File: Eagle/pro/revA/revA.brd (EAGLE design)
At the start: 100 x 100 mm, 24 parts, among them Q1 20MHz

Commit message: simplify
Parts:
- added C5, C7, C8, C9: (no value), SparkFun:0805
- added R11, R12, R13: (no value), SparkFun:1206
- added R5: 100K, SparkFun:1206
- added U$4: LM393, SparkFun:SO08
- added U1: MCP42XXX, SparkFun:SO014
- added X1: USB-MB-H, SparkFun:USB-MB-H
- C4, C6: value 22pF -> (none)
- R10: value 100K -> (none)
- U$2: value LM393 -> AUDIO-JACKPTH; device SparkFun:SO08 -> SparkFun:AUDIO-JACK
- moved R8 94.9 mm to (0.00, -23.0)
- moved C6 92.7 mm to (-13.0, -30.0)
- moved R7 85.5 mm to (0.00, -19.0)
- moved C4 80.4 mm to (-2.00, -15.0), turned to 0 degrees
- moved U$2 80.0 mm to (4.00, 20.0)
- moved R6 53.4 mm to (3.00, -15.0)
- moved R10 39.8 mm to (48.0, 46.0)
- moved C2 32.4 mm to (47.0, 13.0), turned to 0 degrees
- moved C3 32.2 mm to (52.0, 13.0), turned to 180 degrees
- moved Q1 21.1 mm to (48.0, 19.0), turned to 0 degrees
- moved R4 16.3 mm to (71.0, 19.0)
- moved U$1 12.0 mm to (82.0, 29.0)
- moved U$3 1.00 mm to (96.0, 20.0)
- turned ATSAM4LS to 270 degrees
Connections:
- new net DIGI_POT_RST: U1.11
- new net DIGI_POT_SHDW: U1.12
- new net DIGI_RES_LEFT: R4.1, U$1.2, U1.7
- new net DIGI_RES_RIGHT: R9.1, U$1.6, U1.8
- new net DIG_POT_CS: U1.1
- new net MISO: ATSAM4LS.25, U1.13
- new net MOSI: ATSAM4LS.26, U1.3
- new net N$13: R13.1
- new net N$14: R12.1
- new net RAW_LEFT: C4.1, U$3.5
- new net RAW_RIGHT: C5.1, U$3.2
- new net SCLK: ATSAM4LS.27, U1.2
- new net USB_D+: ATSAM4LS.47, R10.1
- new net USB_D-: ATSAM4LS.46, R11.1
- new net V+: U$4.8
- new net V-: U$4.4
- new net VCC: R5.2, R8.2, U$1.8, U1.14, X1.VBUS
- net GND: now also C7.2, R7.1, U$1.4, U$2.1, U1.10, U1.4, U1.5, U1.6, U1.9, X1.GND; no longer C4.2, R10.1
- net N$10: now also C6.1, R13.2, U$4.3; no longer U$1.4, U$2.4
- net N$11: now also C7.1, R12.2, U$4.5; no longer U$1.8, U$2.8
- net N$12: now also C8.2, U$2.5; no longer U$2.3, U$3.2
- net N$3: now also R11.2, X1.D-; no longer U$2.5, U$3.5
- net N$4: now also R10.2, X1.D+; no longer R4.1, R6.2, U$1.2
- net N$5: now also C5.2, R7.2; no longer C6.1
- net N$6: now also C4.2, R5.1, R6.2; no longer C4.1, R7.1
- net N$7: now also C9.1, U$4.6, U$4.7; no longer R8.2, U$2.6, U$2.7
- net N$8: now also C9.2; no longer R7.2, U$2.1
- net N$9: now also C8.1, U$4.1, U$4.2; no longer R10.2, R9.1, U$1.6

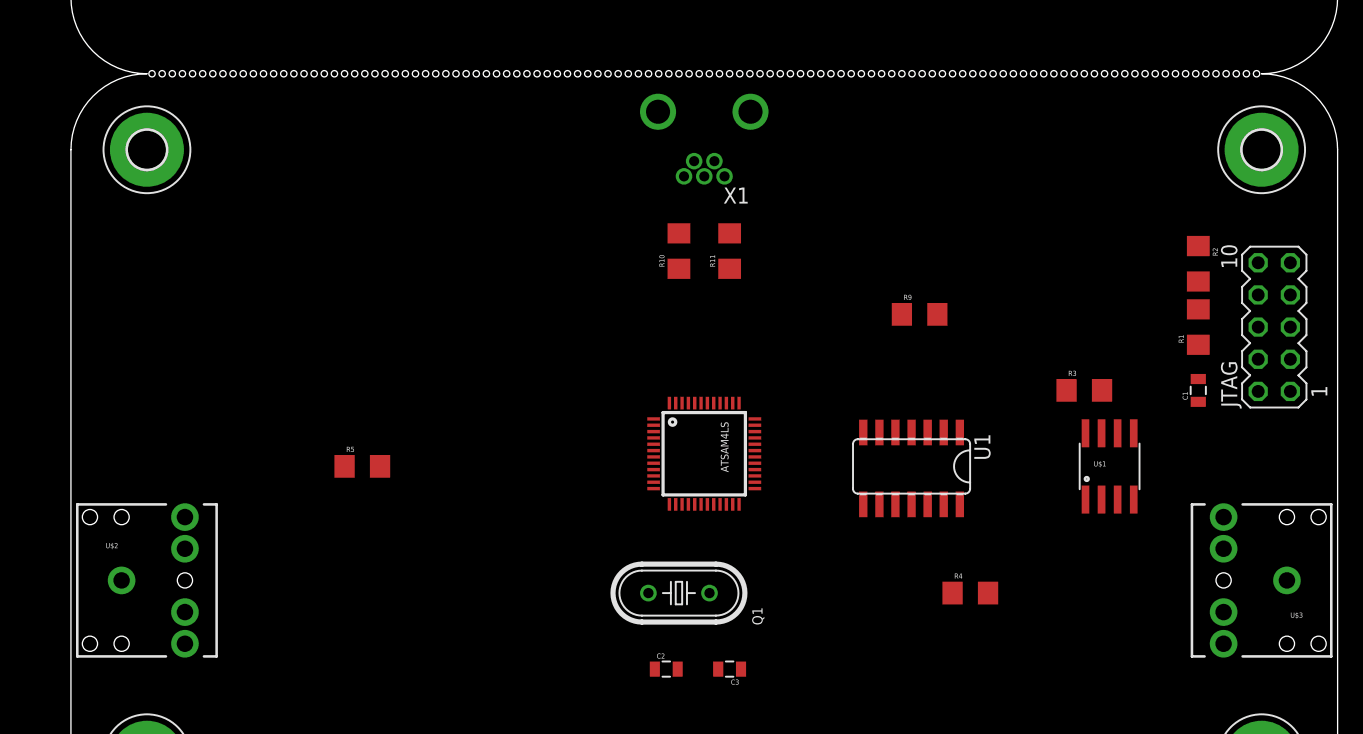
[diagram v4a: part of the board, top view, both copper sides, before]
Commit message: leave jack at the back
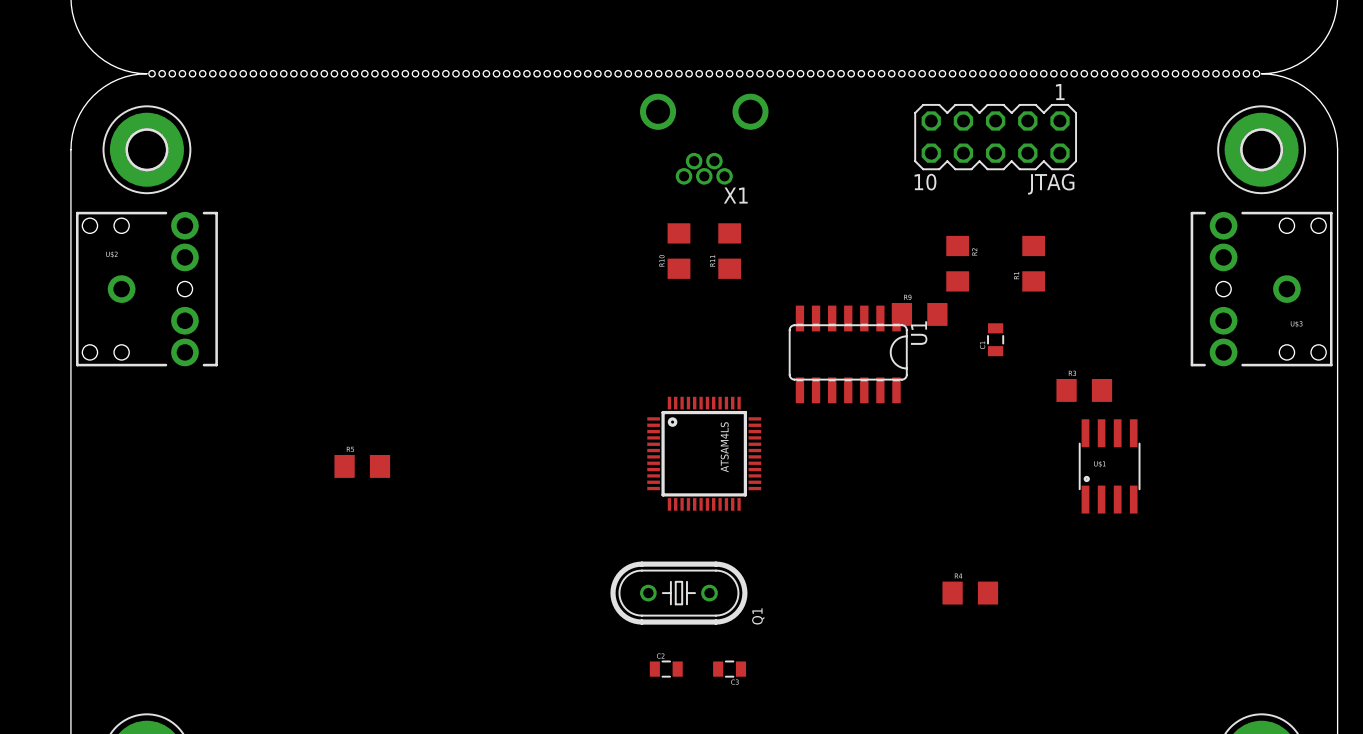
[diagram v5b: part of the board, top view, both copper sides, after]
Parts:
- moved JTAG 26.6 mm to (73.0, 55.0), turned to 180 degrees
- moved U$2 23.0 mm to (4.00, 43.0)
- moved U$3 23.0 mm to (96.0, 43.0)
- moved R2 19.0 mm to (70.0, 45.0)
- moved C1 16.5 mm to (73.0, 39.0)
- moved R1 13.9 mm to (76.0, 45.0)
- moved U1 10.3 mm to (62.0, 38.0)

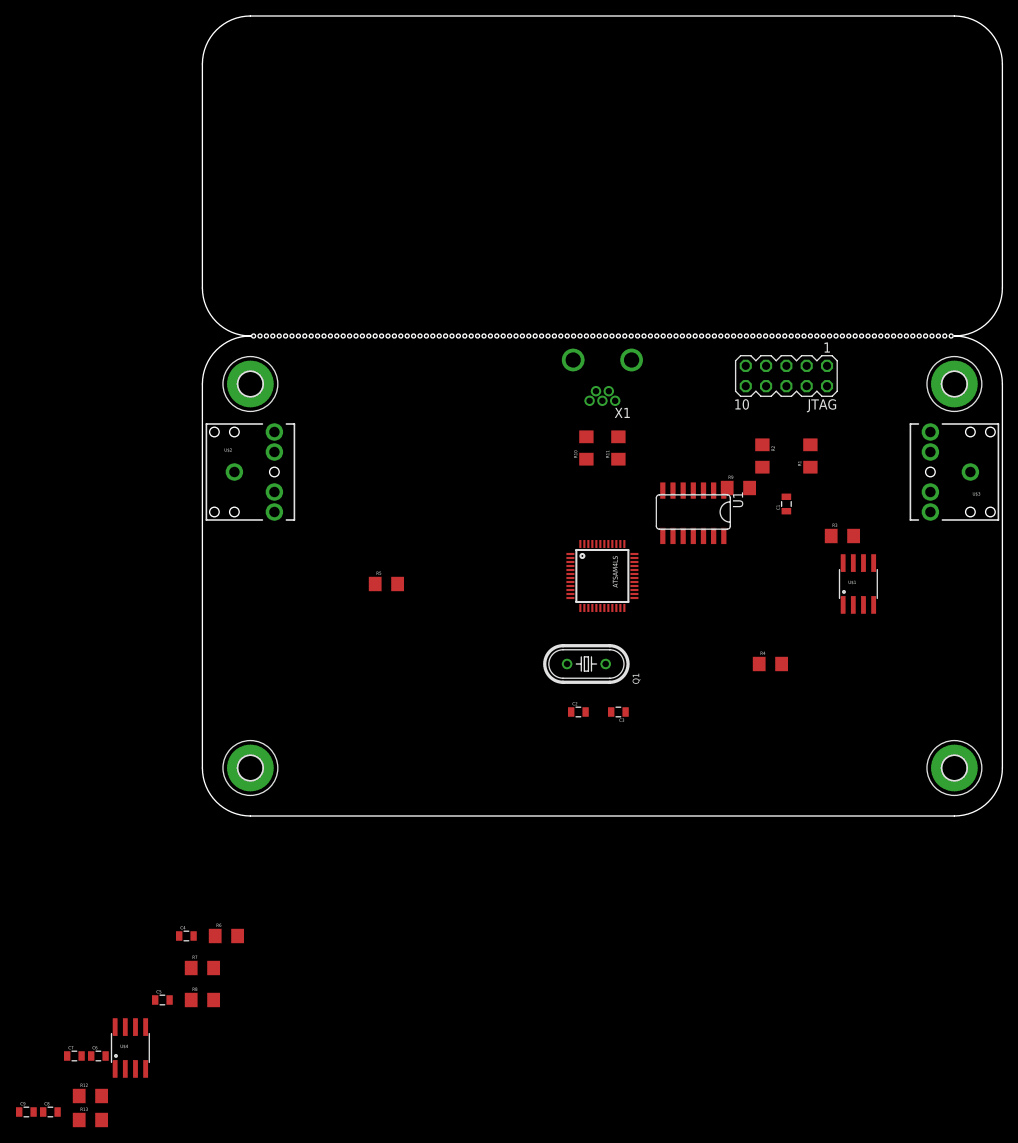
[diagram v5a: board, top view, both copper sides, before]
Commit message: sch done now routing
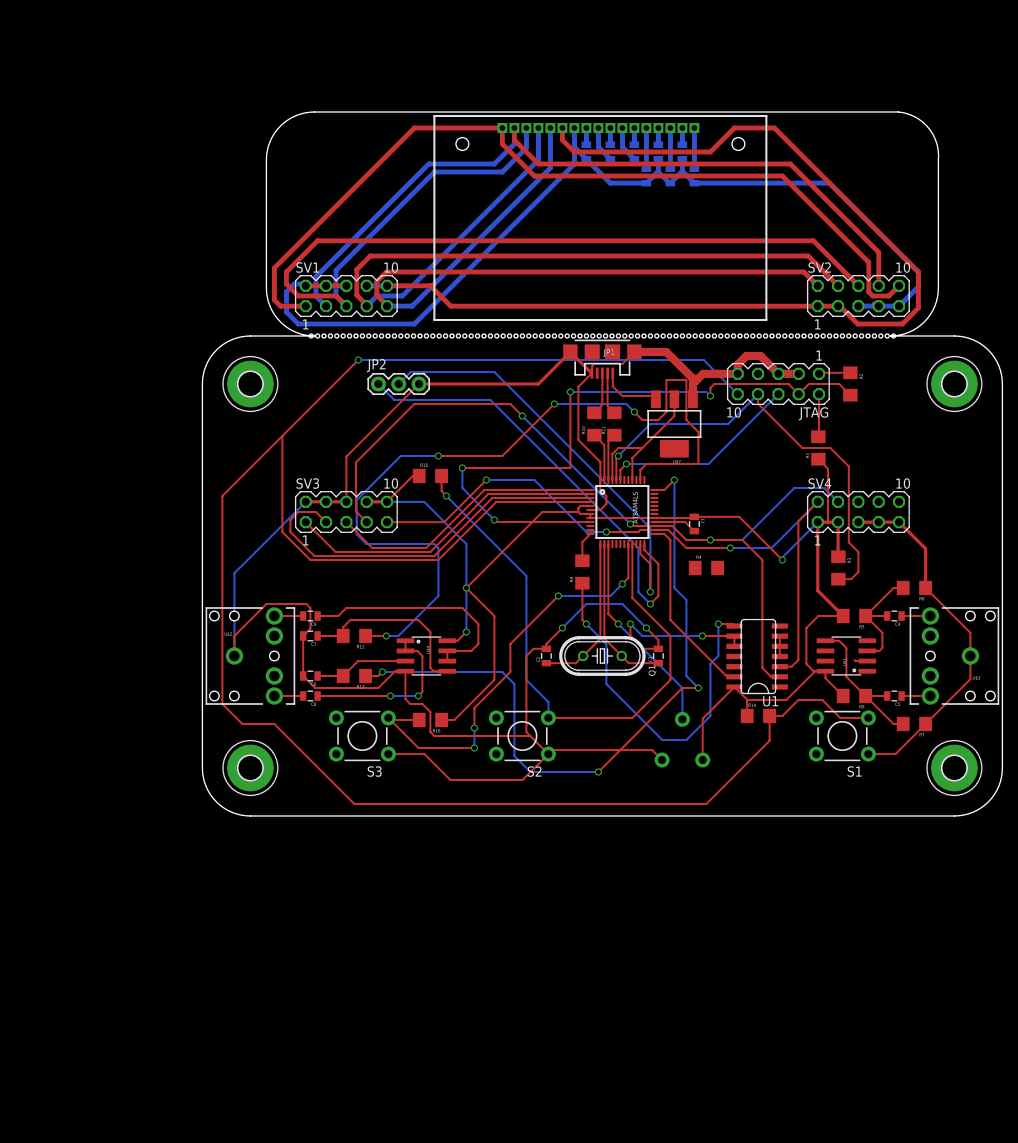
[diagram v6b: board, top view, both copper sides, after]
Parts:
- removed X1: USB-MB-H, SparkFun:USB-MB-H
- added C10, C11, C12, C13, C14, C15, C16, C17: 100nF, SparkFun:0805
- added JP1: USB-MICROB, SparkFun-Connectors:USB-MICROB
- added JP2: JUMPER-3PTH, SparkFun:1X03
- added R14, R15, R16: 100K, SparkFun:1206
- added S1, S2, S3: SWITCH-MOMENTARY-2PTH, SparkFun:TACTILE-PTH
- added SV1, SV2, SV3, SV4: (no value), con-lstb:MA05-2
- added U$5: NHD_128X32, newhaven:NHD_128X32
- added U$6: POTTRIM, SparkFun:TRIM_POT
- added U$7: V_REG_317SMD, SparkFun:SOT223
- C4, C5, C8, C9: value (none) -> 100nF
- C6, C7: value (none) -> 22pF
- R10, R11: value (none) -> 68R
- R12, R13: value (none) -> 330K
- moved C5 99.1 mm to (86.5, 15.0), turned to 180 degrees
- moved C4 97.1 mm to (86.5, 25.0), turned to 180 degrees
- moved R6 96.4 mm to (89.0, 28.5), turned to 180 degrees
- moved R7 94.1 mm to (89.0, 11.5), turned to 180 degrees
- moved R8 89.9 mm to (81.5, 15.0), turned to 180 degrees
- moved C9 71.4 mm to (13.5, 25.0), turned to 180 degrees
- moved R12 66.3 mm to (19.0, 22.5), turned to 180 degrees
- moved R13 64.6 mm to (19.0, 17.5), turned to 180 degrees
- moved U$4 61.4 mm to (28.0, 20.0), turned to 270 degrees
- moved C8 61.3 mm to (13.5, 15.0), turned to 180 degrees
- moved C7 60.2 mm to (13.5, 22.5), turned to 180 degrees
- moved R5 58.6 mm to (81.5, 25.0), turned to 180 degrees
- moved C6 54.4 mm to (13.5, 17.5), turned to 180 degrees
- moved U$2 23.0 mm to (4.00, 20.0)
- moved U$3 23.0 mm to (96.0, 20.0)
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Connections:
- removed net 3.3V: C1.1, JTAG.1, R1.1, R2.1, R3.1
- removed net DIGI_POT_RST: U1.11
- removed net DIGI_POT_SHDW: U1.12
- removed net V+: U$4.8
- removed net V-: U$4.4
- new net DAC_LEFT: ATSAM4LS.36, R13.1
- new net DAC_RIGHT: ATSAM4LS.38, R12.1
- new net DIG_POT_RST: ATSAM4LS.42, U1.11
- new net DIG_POT_SHDW: ATSAM4LS.41, U1.12
- new net LCD_AD: ATSAM4LS.1, SV3.5, SV4.6
- new net LCD_CS: ATSAM4LS.2, SV3.1, SV4.10
- new net LCD_RST: ATSAM4LS.3, SV3.3, SV4.8
- new net MCU_IN: ATSAM4LS.23, JP2.2
- new net MCU_OUT: ATSAM4LS.24, JP2.1
- new net N$15: C10.1, U$5.1
- new net N$16: C11.1, U$5.2
- new net N$17: C12.1, U$5.3
- new net N$18: C13.1, U$5.4
- new net N$19: C14.1, U$5.5
- new net N$20: ATSAM4LS.20, R16.2, S3.3
- new net N$21: SV1.10, SV1.8, SV2.1, SV2.3, U$5.12
- new net N$22: C10.2, C11.2, C12.2, C13.2, C14.2, C17.2, SV1.2, SV1.4, SV1.6, SV2.5, SV2.7, SV2.9, U$5.11
- new net N$23: C15.2, U$5.6
- new net N$24: C15.1, U$5.7
- new net N$25: C16.2, U$5.8
- new net N$26: C16.1, U$5.9
- new net N$27: C17.1, U$5.10
- new net N$28: SV1.1, SV2.10, U$5.17
- new net N$29: SV1.3, SV2.8, U$5.16
- new net N$30: SV1.5, SV2.6, U$5.15
- new net N$31: SV1.7, SV2.4, U$5.14
- new net N$32: SV1.9, SV2.2, U$5.13
- new net N$33: JP1.VBUS, U$7.3
- net DIG_POT_CS: now also ATSAM4LS.39
- net GND: now also ATSAM4LS.17, ATSAM4LS.28, ATSAM4LS.48, ATSAM4LS.6, JP1.GND, JP1.MT1, JP1.MT2, JP2.3, S1.1, S2.1, S3.1, SV3.2, SV3.4, SV3.6, SV4.5, SV4.7, SV4.9, U$4.4, U$6.2, U$7.1; no longer X1.GND
- net MOSI: now also SV3.9, SV4.2
- net N$13: now also ATSAM4LS.15, U$6.1; no longer R13.1
- net N$14: now also ATSAM4LS.21, R15.2, S2.3; no longer R12.1
- net N$3: now also JP1.D-; no longer X1.D-
- net N$4: now also JP1.D+; no longer X1.D+
- net NRESET: now also R14.2, S1.3
- net SCLK: now also SV3.7, SV4.4
- net VCC: now also ATSAM4LS.18, ATSAM4LS.19, ATSAM4LS.29, ATSAM4LS.40, ATSAM4LS.45, ATSAM4LS.5, ATSAM4LS.7, ATSAM4LS.8, C1.1, JTAG.1, R1.1, R14.1, R15.1, R16.1, R2.1, R3.1, SV3.10, SV3.8, SV4.1, SV4.3, U$4.8, U$6.3, U$7.2; no longer X1.VBUS
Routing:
- net GND: track 0.00 -> 333.1 mm, vias 0 -> 4
- net NRESET: track 0.00 -> 248.2 mm, vias 0 -> 1
- net VCC: track 0.00 -> 205.1 mm, vias 0 -> 3
- net N$21: track 0.00 -> 132.2 mm
- net N$22: track 0.00 -> 126.6 mm
- net N$30: track 0.00 -> 123.2 mm
- net N$28: track 0.00 -> 106.1 mm
- net SCLK: track 0.00 -> 105.4 mm, vias 0 -> 3
- net DAC_RIGHT: track 0.00 -> 103.7 mm, vias 0 -> 4
- net N$31: track 0.00 -> 100.5 mm
- net N$29: track 0.00 -> 94.9 mm
- net N$32: track 0.00 -> 92.5 mm
- net DAC_LEFT: track 0.00 -> 86.9 mm, vias 0 -> 4
- net MOSI: track 0.00 -> 85.6 mm, vias 0 -> 3
- net TCK: track 0.00 -> 81.3 mm, vias 0 -> 4
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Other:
- board size 100 x 100 mm -> 100 x 88 mm

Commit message: all routed
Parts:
- moved R15 36.2 mm to (60.5, 25.5), turned to 180 degrees
- moved R4 21.0 mm to (42.0, 30.5), turned to 90 degrees
- moved R3 18.6 mm to (68.5, 46.0), turned to 90 degrees
- moved R2 9.71 mm to (75.5, 46.0), turned to 90 degrees
- moved R6 7.50 mm to (81.5, 28.5), turned to 0 degrees
- moved R1 5.00 mm to (72.0, 46.0)
- moved R14 4.30 mm to (73.0, 10.0), turned to 270 degrees
- moved R7 2.50 mm to (87.0, 10.0), turned to 90 degrees
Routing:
- net LCD_AD: track 34.8 -> 192.3 mm, vias 0 -> 1
- net LCD_CS: track 40.1 -> 193.0 mm
- net LCD_RST: track 48.6 -> 201.3 mm
- net GND: track 333.1 -> 463.1 mm, vias 4 -> 9
- net AUDIO_LEFT: track 0.00 -> 94.9 mm, vias 0 -> 2
- net DIG_POT_CS: track 0.00 -> 78.9 mm, vias 0 -> 4
- net DIGI_RES_LEFT: track 1.67 -> 80.4 mm, vias 0 -> 4
- net AUDIO_RIGHT: track 3.76 -> 78.6 mm, vias 0 -> 2
- net VCC: track 205.1 -> 270.9 mm, vias 3 -> 6
- net TMS: track 5.36 -> 70.5 mm, vias 0 -> 4
- net DIGI_RES_RIGHT: track 45.0 -> 88.3 mm, vias 2 -> 5
- net DIG_POT_RST: track 0.00 -> 34.8 mm, vias 0 -> 4
- net N$14: track 72.0 -> 39.8 mm, vias 1 -> 0
- net DIG_POT_SHDW: track 0.00 -> 30.8 mm, vias 0 -> 2
- net TDI: track 56.1 -> 29.5 mm
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
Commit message: bilk wires
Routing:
- net VCC: track 270.9 -> 257.3 mm, vias 6 -> 3
- net DIGI_RES_LEFT: track 80.4 -> 70.5 mm
- net AUDIO_RIGHT: track 78.6 -> 69.5 mm
- net GND: track 463.1 -> 455.2 mm, vias 9 -> 7
- net N$13: track 25.8 -> 30.5 mm
- net TCK: track 85.5 -> 82.5 mm
- net MOSI: track 83.8 -> 81.4 mm
- net TMS: track 70.5 -> 68.8 mm
- net N$20: track 50.8 -> 50.0 mm
- net DIGI_RES_RIGHT: track 88.3 -> 89.0 mm
